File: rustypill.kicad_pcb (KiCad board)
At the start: 2 copper layers, 69 x 48 mm, 49 parts, among them IC1 DS3231, J1 USB, J2 PROG, J3 GPIOB, J4 GPIOA, J5 LCD1602, J6 IDC_10P, M2 MountingHole_2.7mm_M2.5, M3 MountingHole_2.7mm_M2.5, M4 MountingHole_2.7mm_M2.5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

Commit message: finish pcb design
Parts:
- moved J1 2.65 mm to (82.0, 138.2)
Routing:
- net GND: track 349.5 -> 344.7 mm, vias 10 -> 12
- net USB_DM: track 5.20 -> 7.87 mm
- net VPP: track 79.9 -> 82.6 mm
- net USB_DP: track 13.9 -> 14.7 mm
- net Net-(C6-Pad1): track 137.3 -> 136.5 mm
- added copper zone on B.Cu, net GND
- added copper zone on F.Cu, net GND
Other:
- board text added: "Rustypill v0.1.0 by Ted"

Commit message: finish v0.1.0
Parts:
- moved  M1 0.61 mm to (71.5, 95.7)
- moved M3 0.61 mm to (71.5, 136.3)
- moved M2 0.40 mm to (133.2, 95.7)
- moved M4 0.40 mm to (133.2, 136.3)
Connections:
- J4 pad 9: A8 -> 32KHZ_IN
- U4 pad 29: A8 -> 32KHZ_IN
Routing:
- net 32KHZ_IN: track 44.5 -> 121.0 mm, vias 1 -> 2
- net A2: track 134.1 -> 66.1 mm, vias 1 -> 2
- net VPP: track 82.6 -> 138.4 mm
- net A11: track 61.1 -> 100.0 mm, vias 1 -> 0
- net A8: track 38.1 -> 0.00 mm, vias 3 -> 0
- net B11: track 68.3 -> 39.3 mm, vias 4 -> 2
- net B12: track 103.4 -> 129.3 mm, vias 2 -> 1
- net A12: track 66.6 -> 91.5 mm, vias 2 -> 0
- net Net-(C6-Pad1): track 136.5 -> 113.8 mm
- net B5: track 107.4 -> 86.5 mm
- net A4: track 92.9 -> 72.6 mm
- net A0: track 102.2 -> 84.3 mm, vias 2 -> 1
- net B3: track 116.3 -> 132.7 mm, vias 2 -> 0
- net B13: track 158.7 -> 143.3 mm, vias 2 -> 3
- net B15: track 73.6 -> 88.7 mm, vias 2 -> 1
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
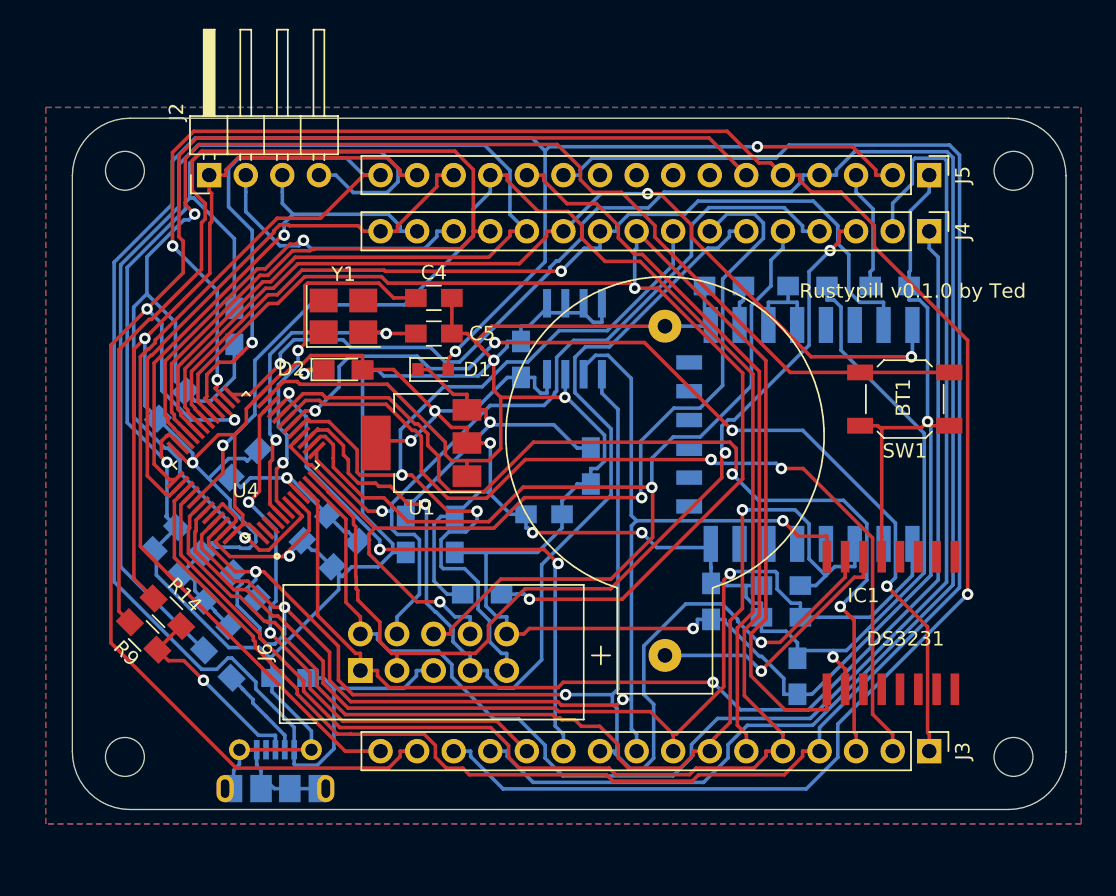
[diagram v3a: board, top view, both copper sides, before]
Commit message: add more I2C features; better placement; etc
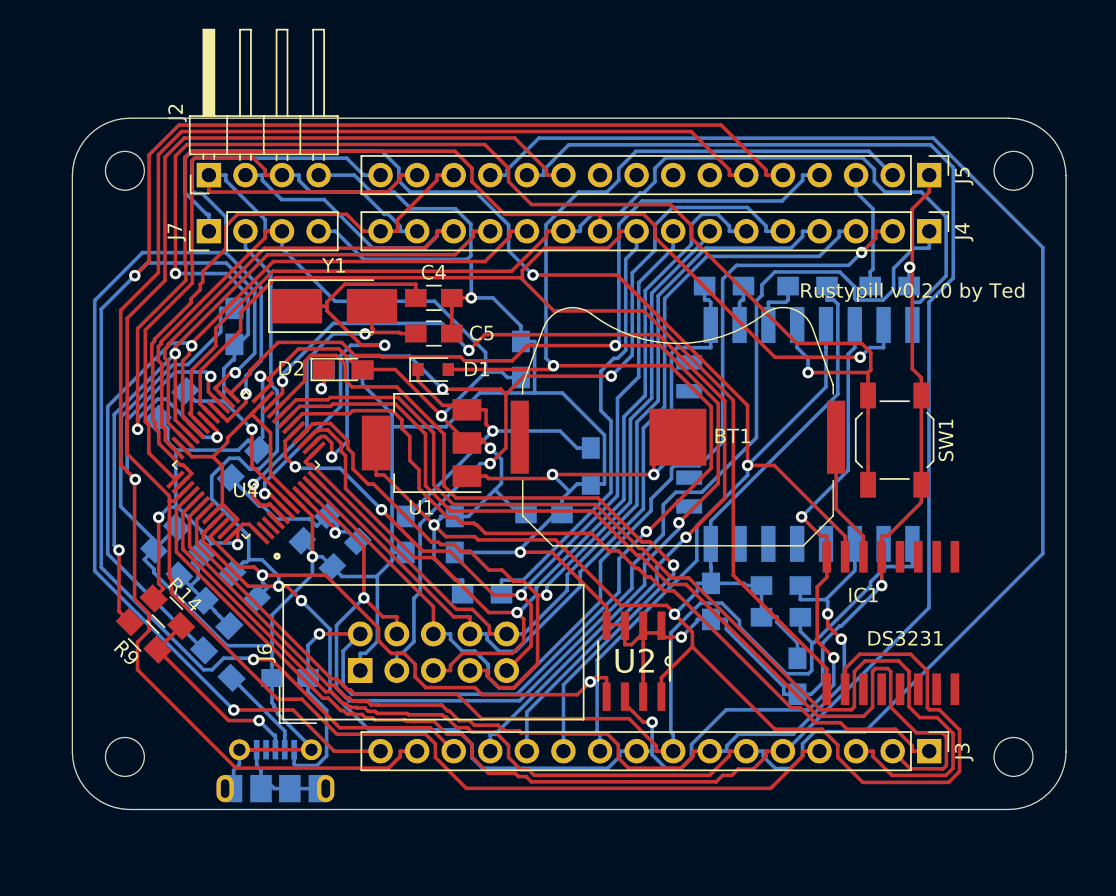
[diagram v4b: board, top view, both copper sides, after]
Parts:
- added J7: I2C, lib:PinHeader_1x04_P2.54mm_Vertical, F.Cu at (77.3, 99.8)
- BT1: footprint Connectors:CR2032H -> lib:my3034_holder
- U2: moved to F.Cu
- Y1: footprint Oscillators:Oscillator_SMD_Abracon_ASE-4pin_3.2x2.5mm_HandSoldering -> Crystals:Crystal_SMD_5032-2pin_5.0x3.2mm_HandSoldering
- moved U2 22.8 mm to (106.8, 129.7)
- moved BT1 15.2 mm to (109.9, 114.2), turned to 180 degrees
- moved SW1 2.93 mm to (125.0, 114.3), turned to 270 degrees
- moved Y1 0.94 mm to (86.0, 105.0)
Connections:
- C6 pad 1: Net-(C6-Pad1) -> IC_RST
- J6 pad 1: A0 -> GND
- J6 pad 10: GND -> A3
- J6 pad 2: A1 -> VPP
- J6 pad 3: A2 -> A4
- J6 pad 4: A3 -> A0
- J6 pad 5: VPP -> A5
- J6 pad 6: A4 -> A1
- J6 pad 7: A5 -> A6
- J6 pad 8: A6 -> A2
- R2 pad 2: Net-(C6-Pad1) -> IC_RST
- SW1 pad 2: Net-(C6-Pad1) -> IC_RST
- U3 pad 18: Net-(R8-Pad1) -> IC_RST
- U3 pad 19: Net-(U3-Pad19) -> B9
- U3 pad 20: Net-(U3-Pad20) -> B8
- U4 pad 7: Net-(C6-Pad1) -> IC_RST
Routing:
- net Net-(C6-Pad1): track 113.8 -> 0.00 mm, vias 2 -> 0
- net IC_RST: track 0.00 -> 107.0 mm, vias 0 -> 3
- net B5: track 86.5 -> 142.8 mm, vias 1 -> 0
- net +3V3: track 219.9 -> 265.9 mm, vias 8 -> 7
- net B9: track 97.4 -> 143.3 mm, vias 3 -> 4
- net A11: track 100.0 -> 60.8 mm, vias 0 -> 1
- net A12: track 91.5 -> 52.9 mm, vias 0 -> 2
- net B12: track 129.3 -> 93.1 mm, vias 1 -> 2
- net B8: track 93.9 -> 126.4 mm, vias 3 -> 5
- net A1: track 101.1 -> 70.6 mm, vias 0 -> 1
- net B11: track 39.3 -> 67.8 mm, vias 2 -> 3
- net GND: track 340.6 -> 313.5 mm, vias 6 -> 8
- net B4: track 104.9 -> 131.6 mm
- net A9: track 64.4 -> 88.4 mm, vias 1 -> 3
- net VPP: track 138.4 -> 114.6 mm, vias 2 -> 3
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- removed copper zone on B.Cu, net GND
- removed copper zone on F.Cu, net GND
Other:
- board text added: "Rustypill v0.2.0 by Ted"
- board text removed: "Rustypill v0.1.0 by Ted"

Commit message: v0.2.0
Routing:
- net A11: track 60.8 -> 102.1 mm, vias 1 -> 0
- net IC_RST: track 107.0 -> 143.9 mm
- net B13: track 125.6 -> 96.2 mm
- net GND: track 313.5 -> 334.8 mm, vias 8 -> 9
- net B14: track 118.0 -> 97.3 mm
- net B2: track 74.9 -> 54.4 mm, vias 0 -> 2
- net B9: track 143.3 -> 123.0 mm, vias 4 -> 6
- net VPP: track 114.6 -> 95.0 mm
- net +3V3: track 265.9 -> 249.8 mm
- net B1: track 70.0 -> 54.2 mm
- net B11: track 67.8 -> 54.0 mm, vias 3 -> 1
- net A10: track 75.3 -> 87.2 mm, vias 0 -> 1
- net A9: track 88.4 -> 78.8 mm
- net B10: track 54.8 -> 46.1 mm, vias 1 -> 3
- net 32KHZ_IN: track 110.7 -> 102.2 mm, vias 0 -> 5
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
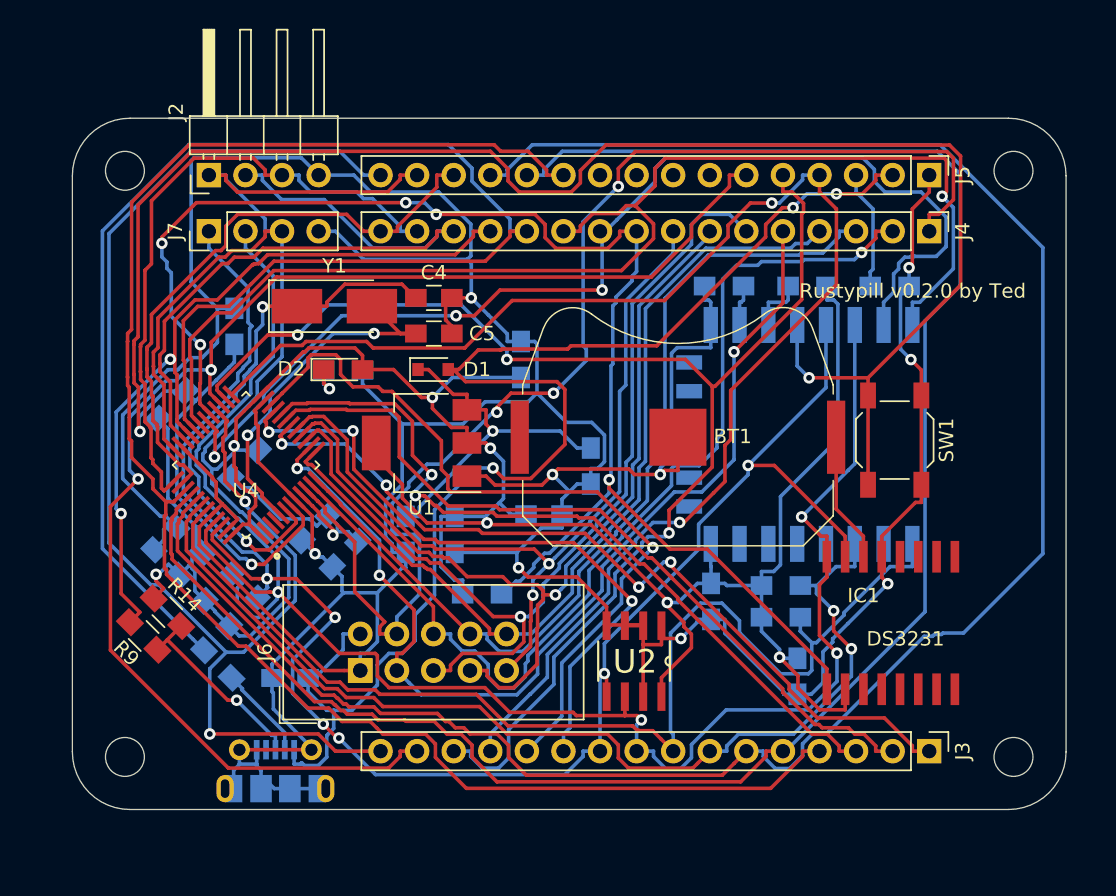
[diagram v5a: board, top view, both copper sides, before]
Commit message: reduce vias
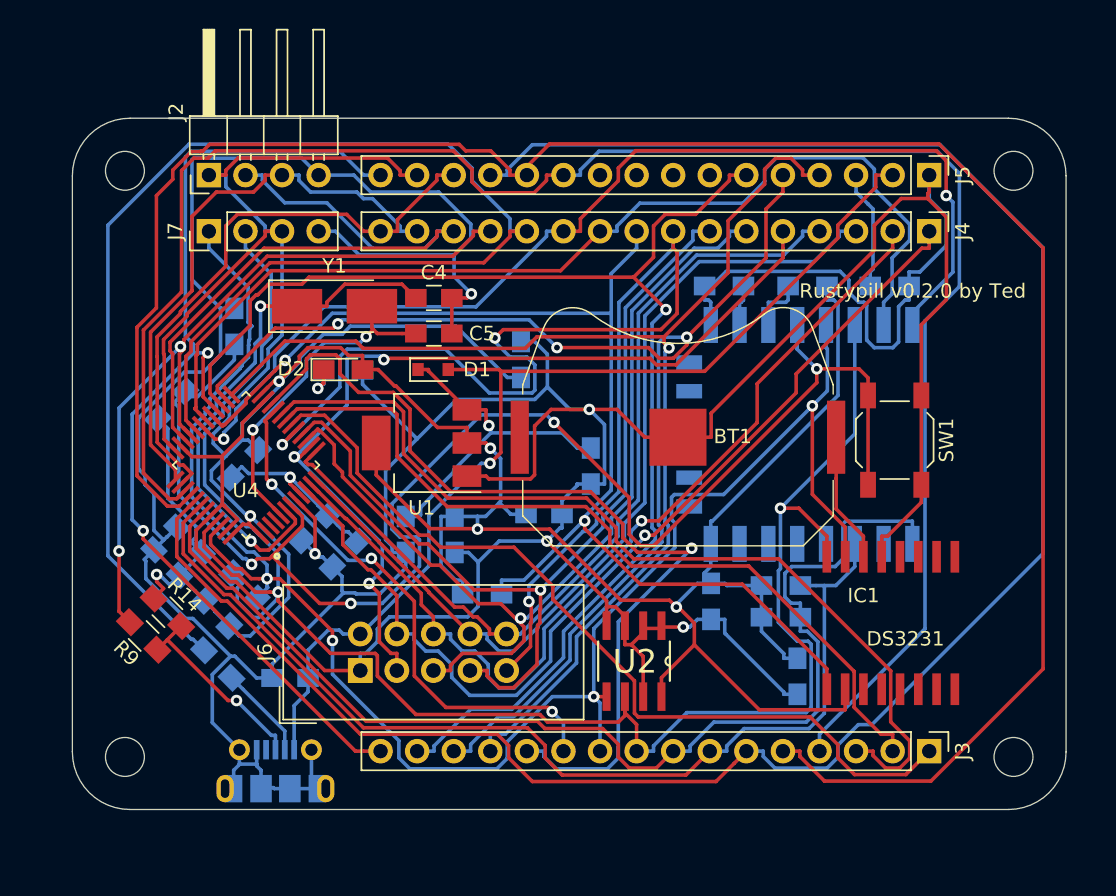
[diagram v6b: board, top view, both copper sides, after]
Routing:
- net GND: track 334.8 -> 378.6 mm, vias 9 -> 5
- net IC_RST: track 143.9 -> 103.3 mm, vias 3 -> 4
- net A7: track 58.8 -> 84.6 mm, vias 2 -> 3
- net B15: track 95.2 -> 71.3 mm
- net VPP: track 95.0 -> 71.9 mm, vias 3 -> 1
- net A0: track 87.3 -> 68.3 mm, vias 3 -> 1
- net 32KHZ_IN: track 102.2 -> 84.4 mm, vias 5 -> 2
- net B3: track 114.9 -> 128.7 mm
- net B12: track 99.9 -> 86.3 mm, vias 2 -> 1
- net B4: track 132.4 -> 145.5 mm
- net A10: track 87.2 -> 76.0 mm, vias 1 -> 2
- net B11: track 54.0 -> 63.8 mm
- net B2: track 54.4 -> 64.0 mm, vias 2 -> 0
- net +3V3: track 249.8 -> 259.3 mm, vias 7 -> 6
- net B10: track 46.1 -> 37.9 mm
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
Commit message: ...
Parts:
- added C16: 100nF, Capacitors_SMD:C_0805_HandSoldering, B.Cu at (74.6, 104.5)
- added C17: 100nF, Capacitors_SMD:C_0805_HandSoldering, B.Cu at (128.1, 128.6)
- added J8: Micro_SD_Card, lib:473340001, F.Cu at (128.6, 131.0)
- added Q1: BC548, TO_SOT_Packages_SMD:SOT-23, F.Cu at (70.3, 102.2)
- added R15: Rbl, Resistors_SMD:R_0805_HandSoldering, B.Cu at (73.1, 106.1)
- added U5: PCF8574, lib:VQFN-16-1EP_3x3mm_P0.5mm_EP1.68x1.68mm, F.Cu at (73.7, 105.1)
- R14, R9: moved to B.Cu
- moved IC1 48.6 mm to (76.2, 130.3)
- moved C11 46.6 mm to (71.6, 128.0), turned to 90 degrees
- moved C12 22.2 mm to (107.0, 129.5), turned to 180 degrees
- moved R14 6.97 mm to (74.6, 133.3)
- moved R9 5.06 mm to (76.3, 131.6)
- moved M3 5.00 mm to (68.5, 140.3)
- moved J3 4.50 mm to (127.3, 140.4)
- moved M4 4.00 mm to (133.2, 140.3)
- moved J1 3.78 mm to (82.0, 142.0)
- moved  M1 3.00 mm to (68.5, 95.7)
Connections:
- J5 pad 11: B3 -> LCD_D4
- J5 pad 12: B4 -> LCD_D5
- J5 pad 13: B5 -> LCD_D6
- J5 pad 14: A15 -> LCD_D7
- J5 pad 16: B15 -> LCD_BL
- J5 pad 4: B12 -> LCD_RS
- J5 pad 5: B13 -> LCD_RW
- J5 pad 6: B14 -> LCD_EN
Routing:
- net GND: track 378.6 -> 0.00 mm, vias 5 -> 0
- net +3V3: track 259.3 -> 0.00 mm, vias 6 -> 0
- net B4: track 145.5 -> 0.00 mm
- net B5: track 143.5 -> 0.00 mm
- net B3: track 128.7 -> 0.00 mm
- net B8: track 128.0 -> 0.00 mm, vias 2 -> 0
- net B9: track 122.2 -> 0.00 mm, vias 4 -> 0
- net IC_RST: track 103.3 -> 0.00 mm, vias 4 -> 0
- net A11: track 100.6 -> 0.00 mm
- net B14: track 91.8 -> 0.00 mm, vias 1 -> 0
- net B13: track 89.6 -> 0.00 mm, vias 3 -> 0
- net B12: track 86.3 -> 0.00 mm, vias 1 -> 0
- net A7: track 84.6 -> 0.00 mm, vias 3 -> 0
- net 32KHZ_IN: track 84.4 -> 0.00 mm, vias 2 -> 0
- net B7: track 80.0 -> 0.00 mm
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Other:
- board size 69 x 48 mm -> 72 x 52 mm

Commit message: ...
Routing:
- net GND: track 0.00 -> 415.1 mm, vias 0 -> 13
- net +3V3: track 0.00 -> 267.0 mm, vias 0 -> 13
- net B8: track 0.00 -> 143.9 mm, vias 0 -> 5
- net B9: track 0.00 -> 133.0 mm, vias 0 -> 2
- net B10: track 0.00 -> 132.7 mm, vias 0 -> 2
- net A0: track 0.00 -> 130.0 mm, vias 0 -> 6
- net IC_RST: track 0.00 -> 123.0 mm, vias 0 -> 10
- net B1: track 0.00 -> 122.0 mm, vias 0 -> 5
- net Net-(C4-Pad1): track 0.00 -> 114.1 mm, vias 0 -> 12
- net B0: track 0.00 -> 113.4 mm, vias 0 -> 5
- net A10: track 0.00 -> 112.3 mm, vias 0 -> 8
- net 32KHZ_IN: track 0.00 -> 107.5 mm, vias 0 -> 7
- net B7: track 0.00 -> 102.1 mm, vias 0 -> 1
- net B6: track 0.00 -> 100.1 mm, vias 0 -> 5
- net B12: track 0.00 -> 99.6 mm, vias 0 -> 4
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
